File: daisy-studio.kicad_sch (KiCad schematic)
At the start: 6 parts, among them J8 Conn_01x04_Pin

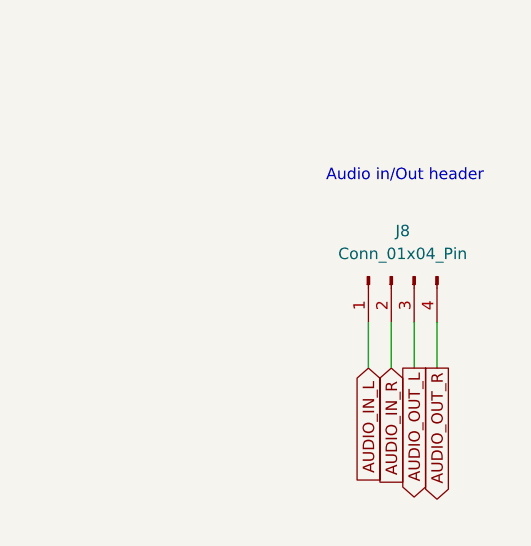
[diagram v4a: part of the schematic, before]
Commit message: introduce daughter board
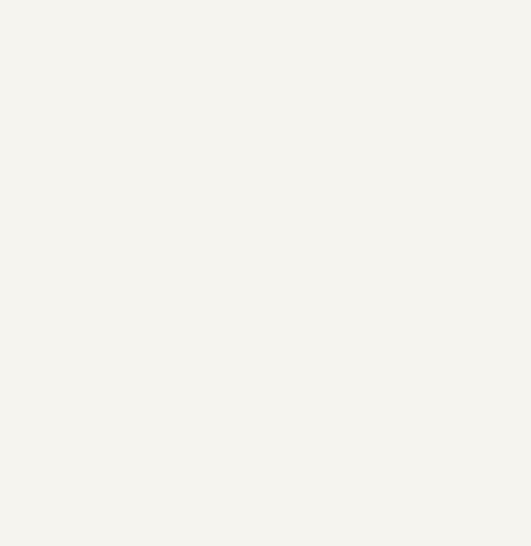
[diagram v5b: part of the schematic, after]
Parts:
- removed J8: Conn_01x04_Pin, Connector_PinHeader_2.54mm:PinHeader_1x04_P2.54mm_Vertical, symbol Connector:Conn_01x04_Pin
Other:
- note removed: "Audio in/Out header"
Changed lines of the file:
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@@
 		(company "Rasheed Abdul-Aziz")
-	)
-	(text "Audio in/Out header\n"
-		(exclude_from_sim no)
-		(at 190.754 96.774 0)
-		(effects
-			(font
-				(size 1.27 1.27)
-			)
-		)
-	)
-	(wire
-		(pts
-			(xy 189.23 113.03) (xy 189.23 118.11)
-		)
-		(stroke
-			(width 0)
-			(type default)
-		)
-	)
-	(wire
-		(pts
-			(xy 194.31 113.03) (xy 194.31 118.11)
-		)
-		(stroke
-			(width 0)
-			(type default)
-		)
-	)
-	(wire
-		(pts
-			(xy 186.69 113.03) (xy 186.69 118.11)
-		)
-		(stroke
-			(width 0)
-			(type default)
-		)
-	)
-	(wire
-		(pts
-			(xy 191.77 113.03) (xy 191.77 118.11)
-		)
-		(stroke
-			(width 0)
-			(type default)
-		)
-	)
-	(global_label "AUDIO_OUT_L"
-		(shape output)
-		(at 191.77 118.11 270)
-		(fields_autoplaced yes)
-		(effects
-			(font
-				(size 1.27 1.27)
-			)
-			(justify right)
-		)
-		(property "Intersheetrefs" "${INTERSHEET_REFS}"
-			(at 191.77 133.3115 90)
-			(effects
-				(font
-					(size 1.27 1.27)
-				)
-				(justify right)
-				(hide yes)
-			)
-		)
-	)
-	(global_label "AUDIO_OUT_R"
-		(shape output)
-		(at 194.31 118.11 270)
-		(fields_autoplaced yes)
-		(effects
-			(font
-				(size 1.27 1.27)
-			)
-			(justify right)
-		)
-		(property "Intersheetrefs" "${INTERSHEET_REFS}"
-			(at 194.31 133.5534 90)
-			(effects
-				(font
-					(size 1.27 1.27)
-				)
-				(justify right)
-				(hide yes)
-			)
-		)
-	)
-	(global_label "AUDIO_IN_R"
-		(shape input)
-		(at 189.23 118.11 270)
-		(fields_autoplaced yes)
-		(effects
-			(font
-				(size 1.27 1.27)
-			)
-			(justify right)
-		)
-		(property "Intersheetrefs" "${INTERSHEET_REFS}"
-			(at 189.23 131.8601 90)
-			(effects
-				(font
-					(size 1.27 1.27)
-				)
-				(justify right)
-				(hide yes)
-			)
-		)
-	)
-	(global_label "AUDIO_IN_L"
-		(shape input)
-		(at 186.69 118.11 270)
-		(fields_autoplaced yes)
-		(effects
-			(font
-				(size 1.27 1.27)
-			)
-			(justify right)
-		)
-		(property "Intersheetrefs" "${INTERSHEET_REFS}"
-			(at 186.69 131.6182 90)
-			(effects
-				(font
-					(size 1.27 1.27)
-				)
-				(justify right)
-				(hide yes)
-			)
-		)
 	)
 	(symbol
@@
 					(unit 1)
 				)
-			)
-		)
-	)
-	(symbol
-		(lib_id "Connector:Conn_01x04_Pin")
-		(at 189.23 107.95 90)
-		(mirror x)
-		(unit 1)
-		(exclude_from_sim no)
-		(in_bom yes)
-		(on_board yes)
-		(dnp no)
-		(property "Reference" "J8"
-			(at 190.5 102.87 90)
-			(effects
-				(font
-					(size 1.27 1.27)
-				)
-			)
-		)
-		(property "Value" "Conn_01x04_Pin"
-			(at 190.5 105.41 90)
-			(effects
-				(font
-					(size 1.27 1.27)
-				)
-			)
-		)
-		(property "Footprint" "Connector_PinHeader_2.54mm:PinHeader_1x04_P2.54mm_Vertical"
-			(at 189.23 107.95 0)
-			(effects
-				(font
-					(size 1.27 1.27)
-				)
-				(hide yes)
-			)
-		)
-		(property "Datasheet" "~"
-			(at 189.23 107.95 0)
-			(effects
-				(font
-					(size 1.27 1.27)
-				)
-				(hide yes)
-			)
-		)
-		(property "Description" "Generic connector, single row, 01x04, script generated"
-			(at 189.23 107.95 0)
-			(effects
-				(font
-					(size 1.27 1.27)
-				)
-				(hide yes)
-			)
-		)
-		(pin "1"
-		)
-		(pin "2"
-		)
-		(pin "3"
-		)
-		(pin "4"
-		)
-		(instances
-			(project "daisy-studio"
-				(path "/55cca6a8-30da-4c13-b2f2-a01401e2b54c"
-					(reference "J8")
-					(unit 1)
-				)

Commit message: starting on output
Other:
- note added: "Non-Coper Mounting Holes"
- moved on the sheet: H1, H2, H3, H4, H5
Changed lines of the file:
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@@
 		(company "Rasheed Abdul-Aziz")
+	)
+	(text "Non-Coper Mounting Holes\n"
+		(exclude_from_sim no)
+		(at 56.388 161.036 0)
+		(effects
+			(font
+				(size 1.27 1.27)
+			)
+		)
 	)
 	(symbol
 		(lib_id "Mechanical:MountingHole")
-		(at 21.59 105.41 0)
+		(at 45.72 176.53 0)
 		(unit 1)
 		(exclude_from_sim no)
@@
 		(fields_autoplaced yes)
 		(property "Reference" "H3"
-			(at 24.13 104.1399 0)
+			(at 48.26 175.2599 0)
 			(effects
 				(font
@@
 		)
 		(property "Value" "MountingHole"
-			(at 24.13 106.6799 0)
+			(at 48.26 177.7999 0)
 			(effects
 				(font
@@
 		)
 		(property "Footprint" "MountingHole:MountingHole_3.2mm_M3"
-			(at 21.59 105.41 0)
+			(at 45.72 176.53 0)
 			(effects
 				(font
@@
 		)
 		(property "Datasheet" "~"
-			(at 21.59 105.41 0)
+			(at 45.72 176.53 0)
 			(effects
 				(font
@@
 		)
 		(property "Description" "Mounting Hole without connection"
-			(at 21.59 105.41 0)
+			(at 45.72 176.53 0)
 			(effects
 				(font
@@
 	(symbol
 		(lib_id "Mechanical:MountingHole")
-		(at 21.59 95.25 0)
+		(at 45.72 166.37 0)
 		(unit 1)
 		(exclude_from_sim no)
@@
 		(fields_autoplaced yes)
 		(property "Reference" "H1"
-			(at 24.13 93.9799 0)
+			(at 48.26 165.0999 0)
 			(effects
 				(font
@@
 		)
 		(property "Value" "MountingHole"
-			(at 24.13 96.5199 0)
+			(at 48.26 167.6399 0)
 			(effects
 				(font
@@
 		)
 		(property "Footprint" "MountingHole:MountingHole_3.2mm_M3"
-			(at 21.59 95.25 0)
+			(at 45.72 166.37 0)
 			(effects
 				(font
@@
 		)
 		(property "Datasheet" "~"
-			(at 21.59 95.25 0)
+			(at 45.72 166.37 0)
 			(effects
 				(font
@@
 		)
 		(property "Description" "Mounting Hole without connection"
-			(at 21.59 95.25 0)
+			(at 45.72 166.37 0)
 			(effects
 				(font
@@
 	(symbol
 		(lib_id "Mechanical:MountingHole")
-		(at 21.59 115.57 0)
+		(at 45.72 186.69 0)
 		(unit 1)
 		(exclude_from_sim no)
@@
 		(fields_autoplaced yes)
 		(property "Reference" "H5"
-			(at 24.13 114.2999 0)
+			(at 48.26 185.4199 0)
 			(effects
 				(font
@@
 		)
 		(property "Value" "MountingHole"
-			(at 24.13 116.8399 0)
+			(at 48.26 187.9599 0)
 			(effects
 				(font
@@
 		)
 		(property "Footprint" "MountingHole:MountingHole_3.2mm_M3"
-			(at 21.59 115.57 0)
+			(at 45.72 186.69 0)
 			(effects
 				(font
@@
 		)
 		(property "Datasheet" "~"
-			(at 21.59 115.57 0)
+			(at 45.72 186.69 0)
 			(effects
 				(font
@@
 		)
 		(property "Description" "Mounting Hole without connection"
-			(at 21.59 115.57 0)
+			(at 45.72 186.69 0)
 			(effects
 				(font
@@
 	(symbol
 		(lib_id "Mechanical:MountingHole")
-		(at 21.59 100.33 0)
+		(at 45.72 171.45 0)
 		(unit 1)
 		(exclude_from_sim no)
@@
 		(fields_autoplaced yes)
 		(property "Reference" "H2"
-			(at 24.13 99.0599 0)
+			(at 48.26 170.1799 0)
 			(effects
 				(font
@@
 		)
 		(property "Value" "MountingHole"
-			(at 24.13 101.5999 0)
+			(at 48.26 172.7199 0)
 			(effects
 				(font
@@
 		)
 		(property "Footprint" "MountingHole:MountingHole_3.2mm_M3"
-			(at 21.59 100.33 0)
+			(at 45.72 171.45 0)
 			(effects
 				(font
@@
 		)
 		(property "Datasheet" "~"
-			(at 21.59 100.33 0)
+			(at 45.72 171.45 0)
 			(effects
 				(font
@@
 		)
 		(property "Description" "Mounting Hole without connection"
-			(at 21.59 100.33 0)
+			(at 45.72 171.45 0)
 			(effects
 				(font
@@
 	(symbol
 		(lib_id "Mechanical:MountingHole")
-		(at 21.59 110.49 0)
+		(at 45.72 181.61 0)
 		(unit 1)
 		(exclude_from_sim no)
@@
 		(fields_autoplaced yes)
 		(property "Reference" "H4"
-			(at 24.13 109.2199 0)
+			(at 48.26 180.3399 0)
 			(effects
 				(font
@@
 		)
 		(property "Value" "MountingHole"
-			(at 24.13 111.7599 0)
+			(at 48.26 182.8799 0)
 			(effects
 				(font
@@
 		)
 		(property "Footprint" "MountingHole:MountingHole_3.2mm_M3"
-			(at 21.59 110.49 0)
+			(at 45.72 181.61 0)
 			(effects
 				(font
@@
 		)
 		(property "Datasheet" "~"
-			(at 21.59 110.49 0)
+			(at 45.72 181.61 0)
 			(effects
 				(font
@@
 		)
 		(property "Description" "Mounting Hole without connection"
-			(at 21.59 110.49 0)
+			(at 45.72 181.61 0)
 			(effects
 				(font
@@
 		)
 		(fill
-			(color 0 0 0 0.0000)
+			(color 0 255 0 1.0000)
 		)
 		(property "Sheetname" "Audio Output"
@@
 		)
 		(fill
-			(color 0 0 0 0.0000)
+			(color 255 153 0 1.0000)
 		)
 		(property "Sheetname" "Seed"
@@
 		)
 		(fill
-			(color 0 0 0 0.0000)
+			(color 255 229 191 1.0000)
 		)
 		(property "Sheetname" "Daughter Board"
@@
 		)
 		(fill
-			(color 194 255 255 1.0000)
+			(color 0 255 255 1.0000)
 		)
 		(property "Sheetname" "Audio Input"

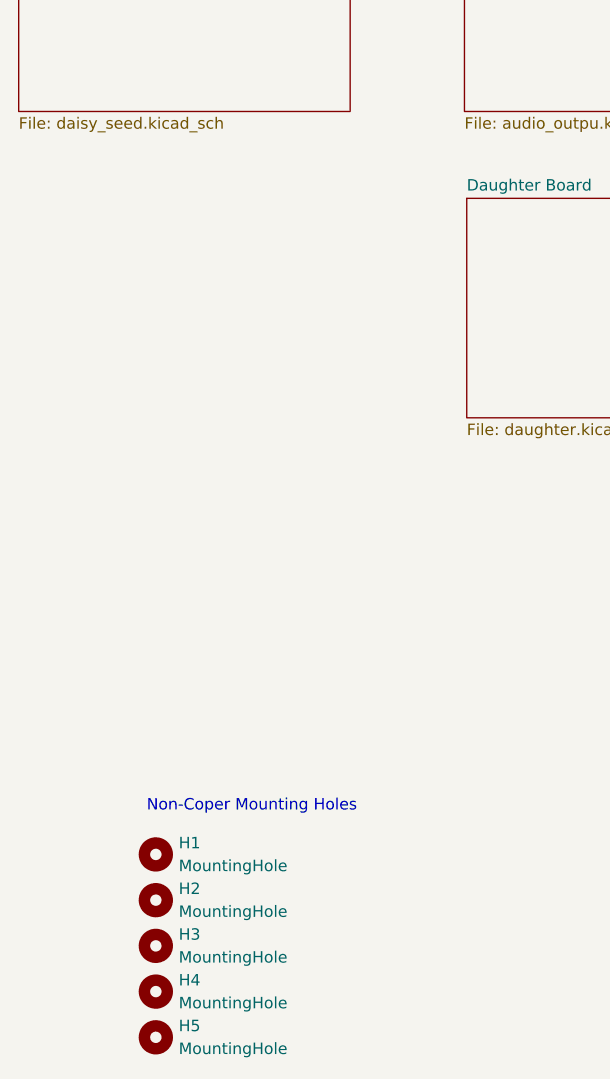
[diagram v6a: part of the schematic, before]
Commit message: daughterboard added
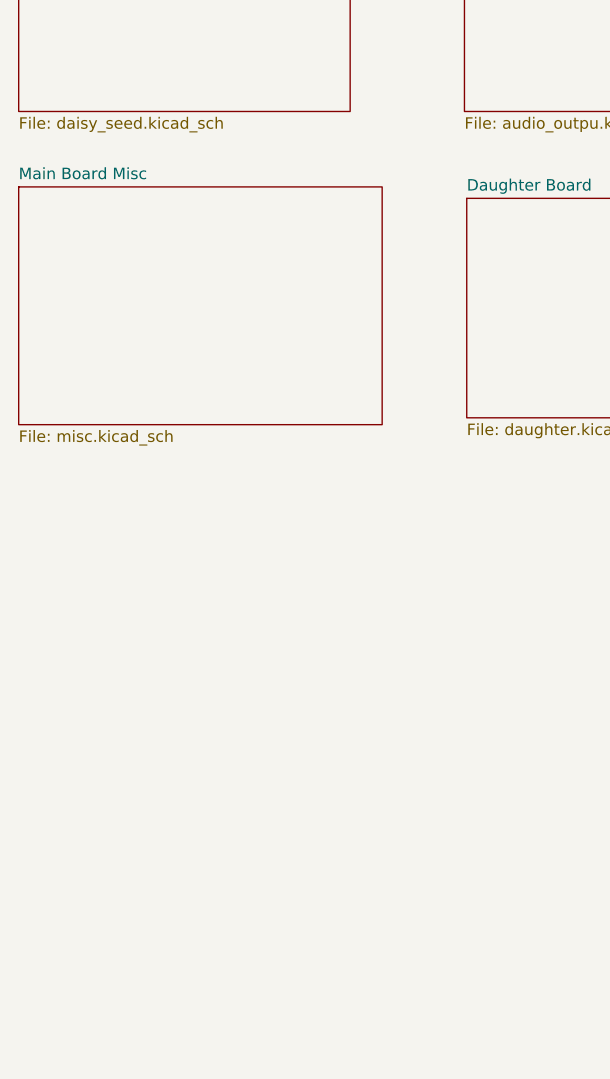
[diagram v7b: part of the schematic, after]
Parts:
- removed H1, H2, H3, H4, H5: MountingHole, MountingHole:MountingHole_3.2mm_M3, symbol Mechanical:MountingHole
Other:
- added sheet Main Board Misc (misc.kicad_sch)
- note removed: "Non-Coper Mounting Holes"

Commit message: WIP adding values
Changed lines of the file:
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@@
 	)
 	(sheet
-		(at 80.01 62.23)
+		(at 172.212 31.75)
 		(size 39.37 21.59)
 		(exclude_from_sim no)
@@
 		)
 		(property "Sheetname" "Audio Output"
-			(at 80.01 61.5184 0)
+			(at 172.212 31.0384 0)
 			(effects
 				(font
@@
 		)
 		(property "Sheetfile" "audio_outpu.kicad_sch"
-			(at 80.01 84.4046 0)
+			(at 172.212 53.9246 0)
 			(effects
 				(font
@@
 	)
 	(sheet
-		(at 30.48 63.5)
+		(at 77.216 31.242)
 		(size 36.83 20.32)
 		(exclude_from_sim no)
@@
 		)
 		(property "Sheetname" "Seed"
-			(at 30.48 62.7884 0)
+			(at 77.216 30.5304 0)
 			(effects
 				(font
@@
 		)
 		(property "Sheetfile" "daisy_seed.kicad_sch"
-			(at 30.48 84.4046 0)
+			(at 77.216 52.1466 0)
 			(effects
 				(font
@@
 	)
 	(sheet
-		(at 80.264 93.472)
+		(at 76.962 61.722)
 		(size 39.116 24.384)
 		(exclude_from_sim no)
@@
 		)
 		(property "Sheetname" "Daughter Board"
-			(at 80.264 92.7604 0)
+			(at 76.962 61.0104 0)
 			(effects
 				(font
@@
 		)
 		(property "Sheetfile" "daughter.kicad_sch"
-			(at 80.264 118.4406 0)
+			(at 76.962 86.6906 0)
 			(effects
 				(font
@@
 	)
 	(sheet
-		(at 78.74 31.75)
+		(at 124.714 31.242)
 		(size 40.64 20.32)
 		(exclude_from_sim no)
@@
 		)
 		(property "Sheetname" "Audio Input"
-			(at 78.74 31.0394 0)
+			(at 124.714 30.5314 0)
 			(effects
 				(font
@@
 		)
 		(property "Sheetfile" "audio.kicad_sch"
-			(at 78.74 52.6646 0)
+			(at 124.714 52.1566 0)
 			(effects
 				(font
@@
 	)
 	(sheet
-		(at 30.48 92.202)
+		(at 30.988 60.96)
 		(size 40.386 26.416)
 		(exclude_from_sim no)
@@
 		)
 		(property "Sheetname" "Main Board Misc"
-			(at 30.48 91.4904 0)
+			(at 30.988 60.2484 0)
 			(effects
 				(font
@@
 		)
 		(property "Sheetfile" "misc.kicad_sch"
-			(at 30.48 119.2026 0)
-			(effects
-				(font
+			(at 30.988 87.9606 0)
+			(effects
+				(font
